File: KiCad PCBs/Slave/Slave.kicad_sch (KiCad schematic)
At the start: 44 parts, among them J1 Screw_Terminal_01x02, J10 AVR-ISP-6, J11 Conn_01x06_Female, J2 Screw_Terminal_01x02, J3 Screw_Terminal_01x02, J4 Screw_Terminal_01x02, J5 Screw_Terminal_01x02, J6 Screw_Terminal_01x02, J7 Screw_Terminal_01x02, J8 Screw_Terminal_01x02, J9 Screw_Terminal_01x02, SW1 SW_DIP_x04, U1 ATmega328P-AU, U2 MAX487ESA+T, U3 ULN2003A, U4 LM358DR2G, Y1 Crystal_GND24

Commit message: Annotated Slave
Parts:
- gave numbers to parts that had none: 22
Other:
- note added: "Reset Switch"
- note removed: "Reset"

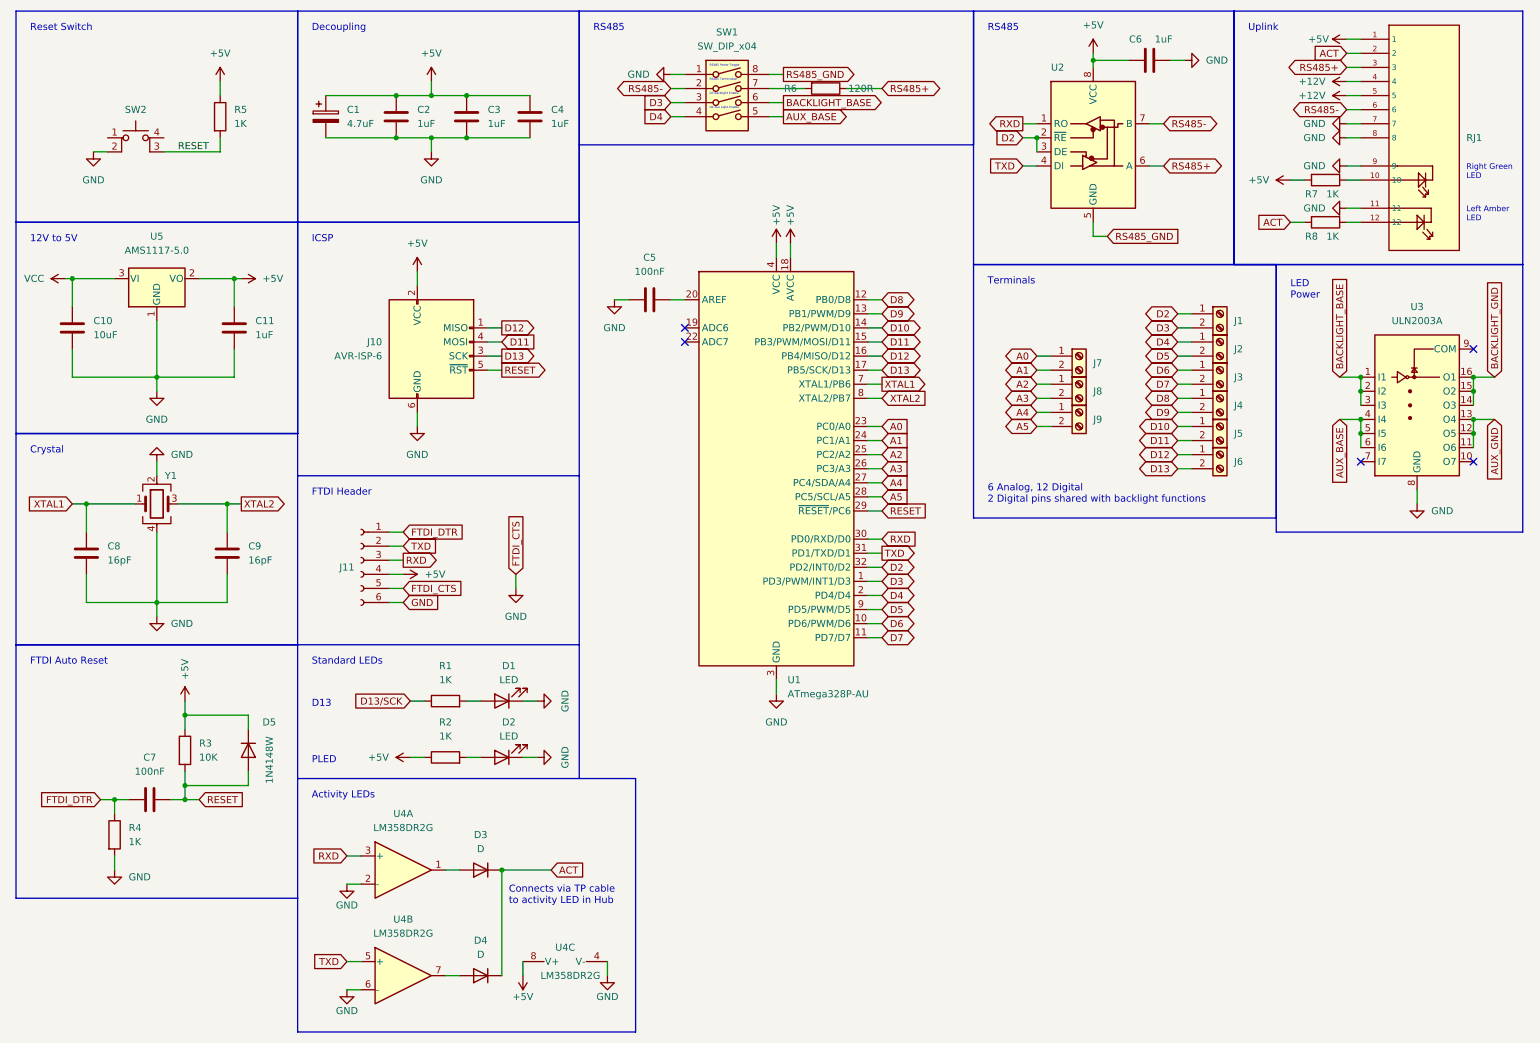
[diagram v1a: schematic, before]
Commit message: Added LED terminals
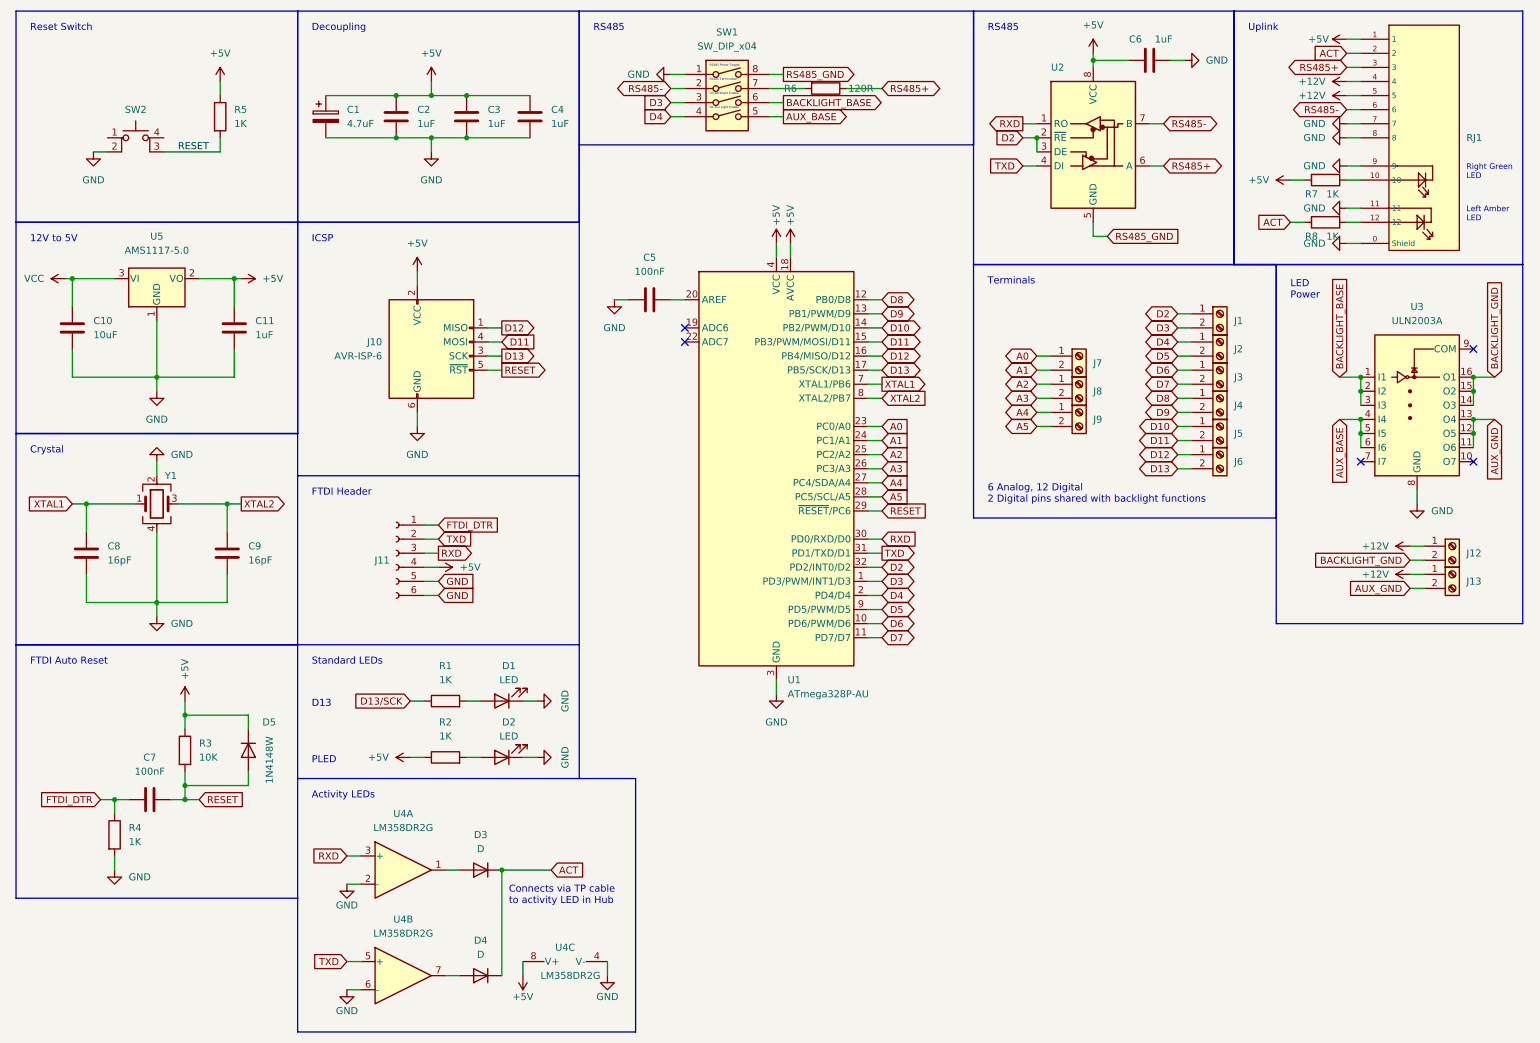
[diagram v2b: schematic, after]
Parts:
- added J12, J13: Screw_Terminal_01x02, A10 KiCad Libraries:CONN-TH_WJ126V-5.0-2P, symbol Connector:Screw_Terminal_01x02
- C10, C11, C7, C8, C9: footprint (none) -> A10 KiCad Libraries:C0402
- D3, D4: footprint (none) -> A10 KiCad Libraries:SOD-123F_L2.8-W1.8-LS3.7-RD
- J1, J2, J3, J4, J5, J6, J7, J8, J9: footprint (none) -> A10 KiCad Libraries:CONN-TH_WJ126V-5.0-2P
- J10: footprint (none) -> Connector_PinHeader_2.54mm:PinHeader_2x03_P2.54mm_Vertical
- J11: footprint (none) -> Connector_PinHeader_2.54mm:PinHeader_1x06_P2.54mm_Vertical
- R5: footprint (none) -> Resistor_SMD:R_0402_1005Metric
- SW1: footprint (none) -> Button_Switch_SMD:SW_DIP_SPSTx04_Slide_9.78x12.34mm_W8.61mm_P2.54mm
- U2: footprint (none) -> A10 KiCad Libraries:SOIC-8_L5.0-W4.0-P1.27-LS6.0-BL
- U3: footprint (none) -> A10 KiCad Libraries:SOP-16_L10.0-W3.9-P1.27-LS6.0-BL
- Y1: footprint (none) -> Crystal:Crystal_SMD_3225-4Pin_3.2x2.5mm
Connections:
- net +12V: now also J12.1 (Pin_1), J13.1 (Pin_1)
- net AUX_GND: now also J13.2 (Pin_2)
- net BACKLIGHT_GND: now also J12.2 (Pin_2)
- net GND: now also RJ1.0 (Shield)
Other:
- moved on the sheet: J11

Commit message: Replaced 4P switch with 2x2P switches because of placement
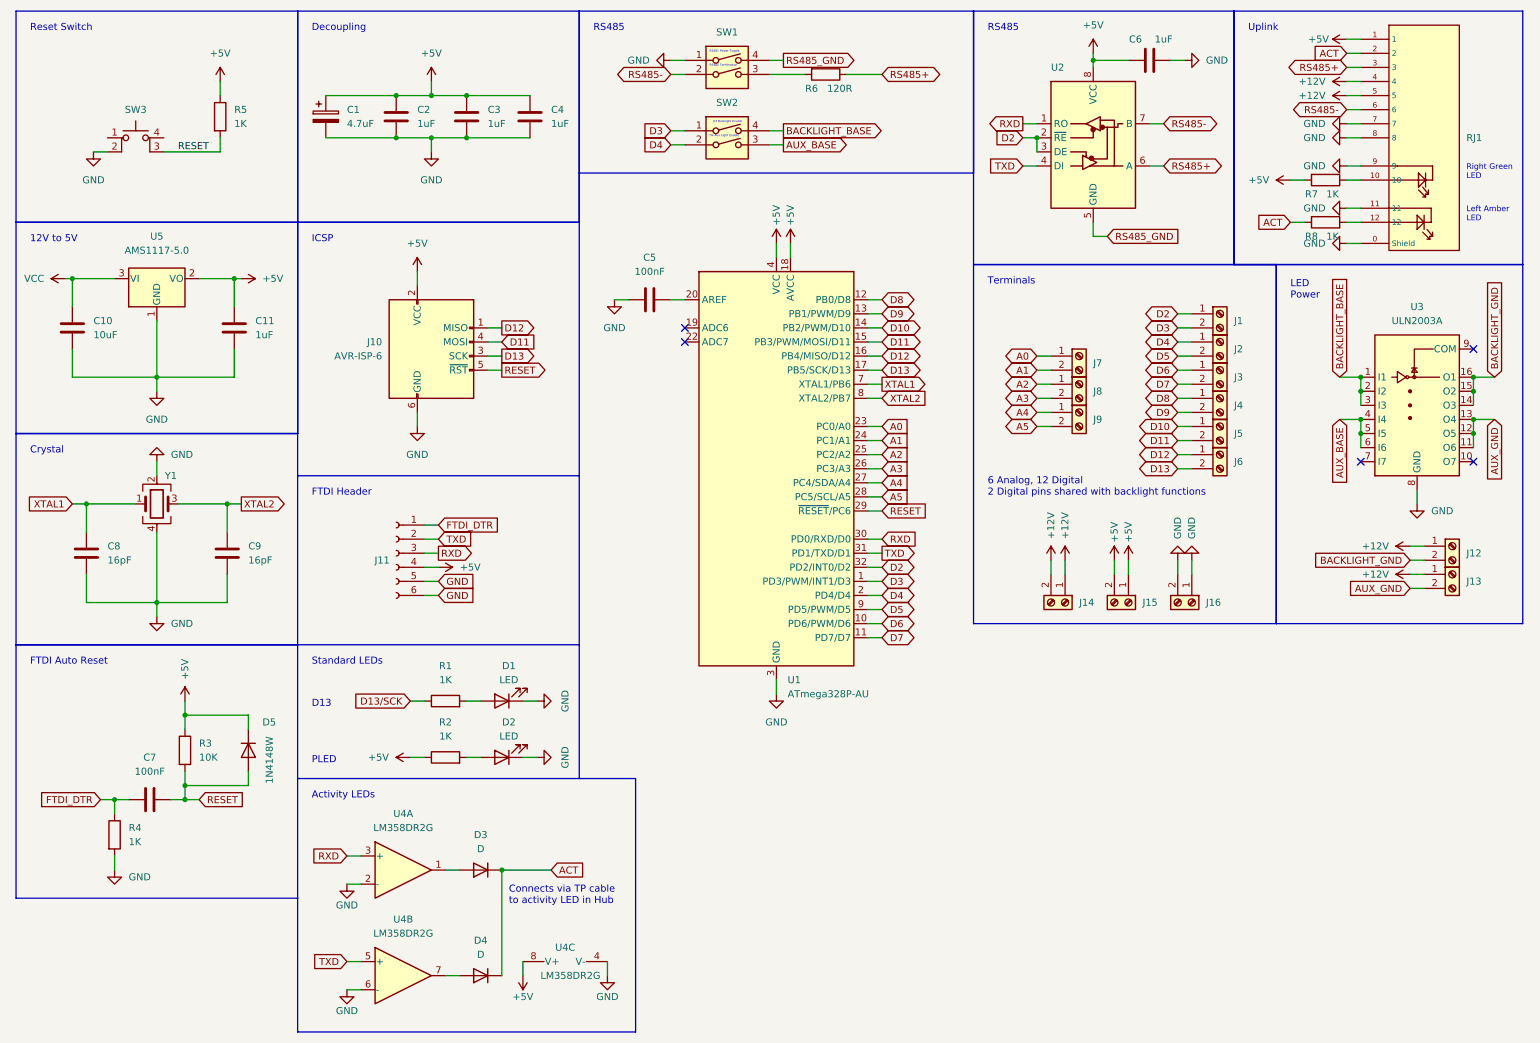
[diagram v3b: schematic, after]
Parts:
- removed SW1: SW_DIP_x04, Button_Switch_SMD:SW_DIP_SPSTx04_Slide_9.78x12.34mm_W8.61mm_P2.54mm, symbol Switch:SW_DIP_x04
- added J14, J15, J16: Screw_Terminal_01x02, A10 KiCad Libraries:CONN-TH_WJ126V-5.0-2P, symbol Connector:Screw_Terminal_01x02
- added SW1, SW2: SW_DIP_x02, A10 KiCad Libraries:SW-SMD_DSHP02TSGER, symbol Switch:SW_DIP_x02
- J11: footprint Connector_PinHeader_2.54mm:PinHeader_1x06_P2.54mm_Vertical -> Connector_PinSocket_2.54mm:PinSocket_1x06_P2.54mm_Vertical
- renumbered SW2 to SW3
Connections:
- net +12V: now also J14.1 (Pin_1), J14.2 (Pin_2)
- net +5V: now also J15.1 (Pin_1), J15.2 (Pin_2)
- net AUX_BASE: now also SW2.3
- net BACKLIGHT_BASE: now also SW2.4
- net D3: now also SW2.1
- net D4: now also SW2.2
- net GND: now also J16.1 (Pin_1), J16.2 (Pin_2), SW1.1
- net RS485-: now also SW1.2
- net RS485_GND: now also SW1.4
- net at R6.2: now also SW1.3
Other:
- moved on the sheet: R6

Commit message: Slave PCB wip
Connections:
- net VCC is gone; now on net +12V: C10.1, U5.3 (VI)
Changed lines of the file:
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@@
     (pin "1")
   )
-  (symbol (lib_id "power:VCC") (at 21.59 60.96 90) (unit 1)
-    (in_bom yes) (on_board yes) (fields_autoplaced)
-    (property "Reference" "#PWR0103" (id 0) (at 25.4 60.96 0)
-      (effects (font (size 1.27 1.27)) hide)
-    )
-    (property "Value" "VCC" (id 1) (at 17.78 60.9599 90)
+  (symbol (lib_id "power:+12V") (at 21.59 60.96 90) (unit 1)
+    (in_bom yes) (on_board yes) (fields_autoplaced)
+    (property "Reference" "#PWR?" (id 0) (at 25.4 60.96 0)
+      (effects (font (size 1.27 1.27)) hide)
+    )
+    (property "Value" "+12V" (id 1) (at 17.78 60.9599 90)
       (effects (font (size 1.27 1.27)) (justify left))
     )
@@
   (symbol (lib_id "power:+12V") (at 199.39 111.76 0) (unit 1)
     (in_bom yes) (on_board yes)
-    (property "Reference" "#PWR?" (id 0) (at 199.39 115.57 0)
+    (property "Reference" "#PWR0143" (id 0) (at 199.39 115.57 0)
       (effects (font (size 1.27 1.27)) hide)
     )
@@
   (symbol (lib_id "power:GND") (at 222.25 111.76 180) (unit 1)
     (in_bom yes) (on_board yes)
-    (property "Reference" "#PWR?" (id 0) (at 222.25 105.41 0)
+    (property "Reference" "#PWR0142" (id 0) (at 222.25 105.41 0)
       (effects (font (size 1.27 1.27)) hide)
     )
@@
   (symbol (lib_id "power:+5V") (at 210.82 111.76 0) (unit 1)
     (in_bom yes) (on_board yes)
-    (property "Reference" "#PWR?" (id 0) (at 210.82 115.57 0)
+    (property "Reference" "#PWR0145" (id 0) (at 210.82 115.57 0)
       (effects (font (size 1.27 1.27)) hide)
     )
@@
   (symbol (lib_id "power:+5V") (at 213.36 111.76 0) (unit 1)
     (in_bom yes) (on_board yes)
-    (property "Reference" "#PWR?" (id 0) (at 213.36 115.57 0)
+    (property "Reference" "#PWR0146" (id 0) (at 213.36 115.57 0)
       (effects (font (size 1.27 1.27)) hide)
     )
@@
   (symbol (lib_id "power:GND") (at 224.79 111.76 180) (unit 1)
     (in_bom yes) (on_board yes)
-    (property "Reference" "#PWR?" (id 0) (at 224.79 105.41 0)
+    (property "Reference" "#PWR0141" (id 0) (at 224.79 105.41 0)
       (effects (font (size 1.27 1.27)) hide)
     )
@@
   (symbol (lib_id "power:+12V") (at 201.93 111.76 0) (unit 1)
     (in_bom yes) (on_board yes)
-    (property "Reference" "#PWR?" (id 0) (at 201.93 115.57 0)
+    (property "Reference" "#PWR0144" (id 0) (at 201.93 115.57 0)
       (effects (font (size 1.27 1.27)) hide)
     )
@@
       (reference "#PWR0102") (unit 1) (value "GND") (footprint "")
     )
-    (path "/194dc9ab-37aa-4cbc-9ef1-587feb771d5b"
-      (reference "#PWR0103") (unit 1) (value "VCC") (footprint "")
-    )
     (path "/bca02340-bac0-4826-b369-7dfd2dbaae17"
       (reference "#PWR0104") (unit 1) (value "GND") (footprint "")
@@
       (reference "#PWR0140") (unit 1) (value "+12V") (footprint "")
     )
+    (path "/c957a2f3-975e-4815-b0db-1d09d756e7e3"
+      (reference "#PWR0141") (unit 1) (value "GND") (footprint "")
+    )
+    (path "/a1518afb-ff06-48aa-b596-25d2f669409c"
+      (reference "#PWR0142") (unit 1) (value "GND") (footprint "")
+    )
     (path "/5d2c4836-7cc2-4e26-b00a-a2f63bc6e343"
+      (reference "#PWR0143") (unit 1) (value "+12V") (footprint "")
+    )
+    (path "/d96b4a54-9706-48ab-a24a-ef8221305958"
+      (reference "#PWR0144") (unit 1) (value "+12V") (footprint "")
+    )
+    (path "/c55abec2-f2b3-4503-aee1-98ee6bd32fca"
+      (reference "#PWR0145") (unit 1) (value "+5V") (footprint "")
+    )
+    (path "/c6931e1c-d659-4f95-891f-5dded99173e1"
+      (reference "#PWR0146") (unit 1) (value "+5V") (footprint "")
+    )
+    (path "/1d7d13da-6155-4f5e-b055-b0667fd2dc2b"
       (reference "#PWR?") (unit 1) (value "+12V") (footprint "")
     )
-    (path "/a1518afb-ff06-48aa-b596-25d2f669409c"
-      (reference "#PWR?") (unit 1) (value "GND") (footprint "")
-    )
-    (path "/c55abec2-f2b3-4503-aee1-98ee6bd32fca"
-      (reference "#PWR?") (unit 1) (value "+5V") (footprint "")
-    )
-    (path "/c6931e1c-d659-4f95-891f-5dded99173e1"
-      (reference "#PWR?") (unit 1) (value "+5V") (footprint "")
-    )
-    (path "/c957a2f3-975e-4815-b0db-1d09d756e7e3"
-      (reference "#PWR?") (unit 1) (value "GND") (footprint "")
-    )
-    (path "/d96b4a54-9706-48ab-a24a-ef8221305958"
-      (reference "#PWR?") (unit 1) (value "+12V") (footprint "")
-    )
